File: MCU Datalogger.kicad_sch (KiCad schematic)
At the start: 0 parts

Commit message: Have added required symbols to the schematic sheets
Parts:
- added BT?: Battery, symbol Device:Battery
- added C? (x4): C, symbol Device:C
- added C?: C_Polarized, symbol Device:C_Polarized
- added D? (x2): LED, symbol Device:LED
- added H? (x4): MountingHole, symbol Mechanical:MountingHole
- added R1, R2, R3, R4, R5, R? (x2): R, symbol Device:R
- added U1, U2: 24LC1025, symbol Memory_EEPROM:24LC1025
- added U?: DS1337S+, SOIC127P600X175-8N, symbol DS1337S_:DS1337S+
- added U?: ATMEGA328P-AU, QFP80P900X900X120-32N, symbol ATMEGA328P-AU:ATMEGA328P-AU
- added Y? (x2): Crystal, symbol Device:Crystal
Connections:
- new net: U?.21 (GND), U?.3 (GND), U?.5 (GND)
- new net: U?.4 (VCC), U?.6 (VCC)
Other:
- added sheet Connectors (connectors.kicad_sch)

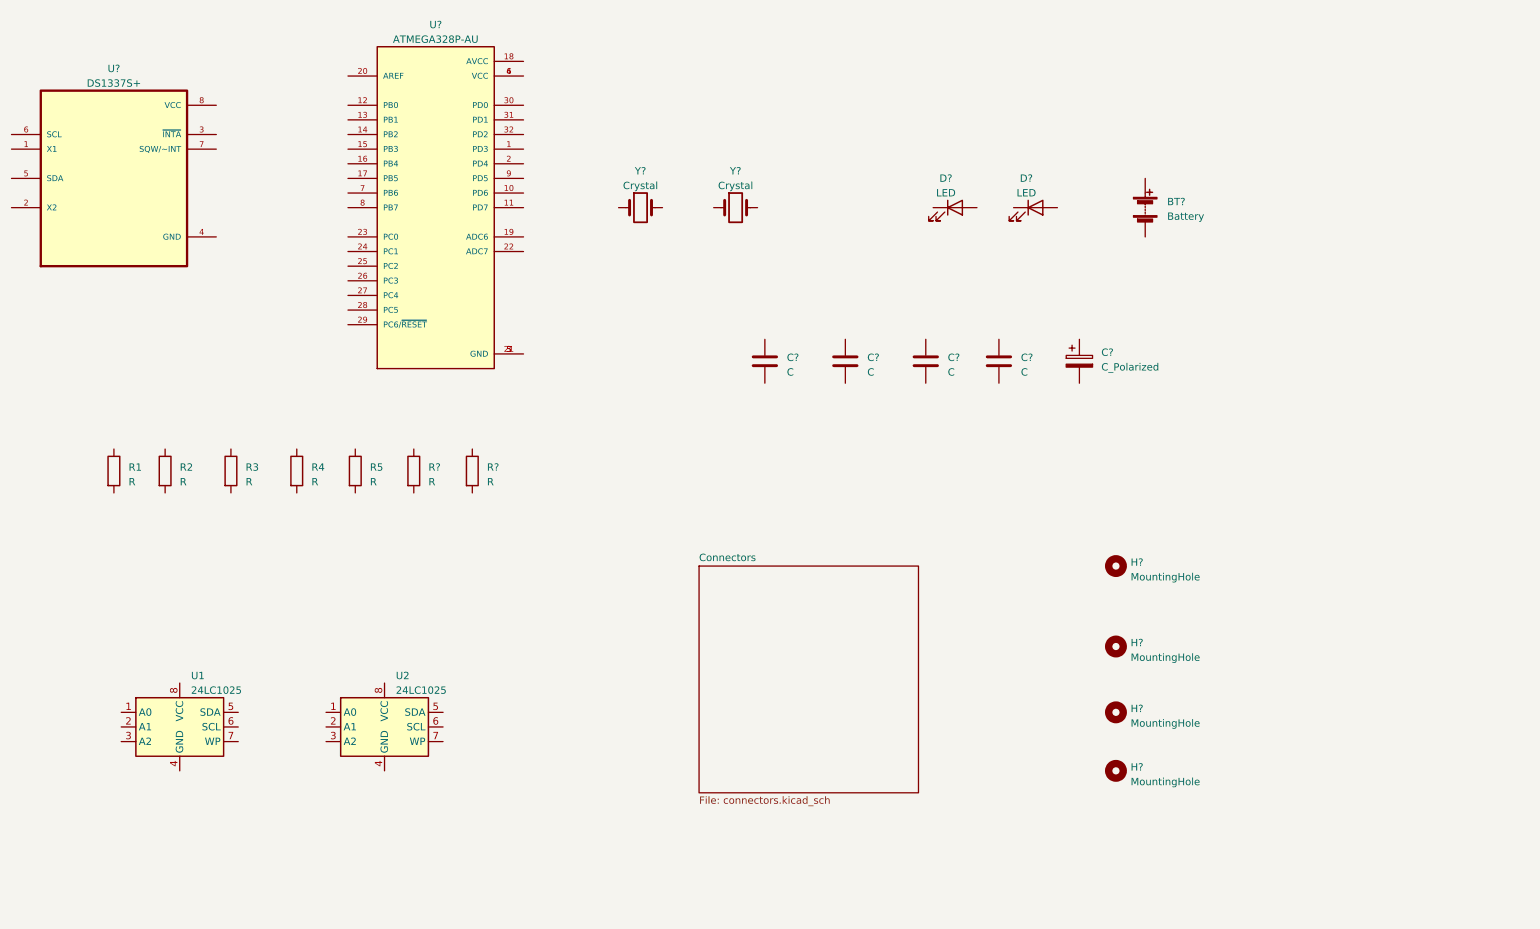
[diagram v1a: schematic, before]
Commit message: Changed locations of symbols (arrange)
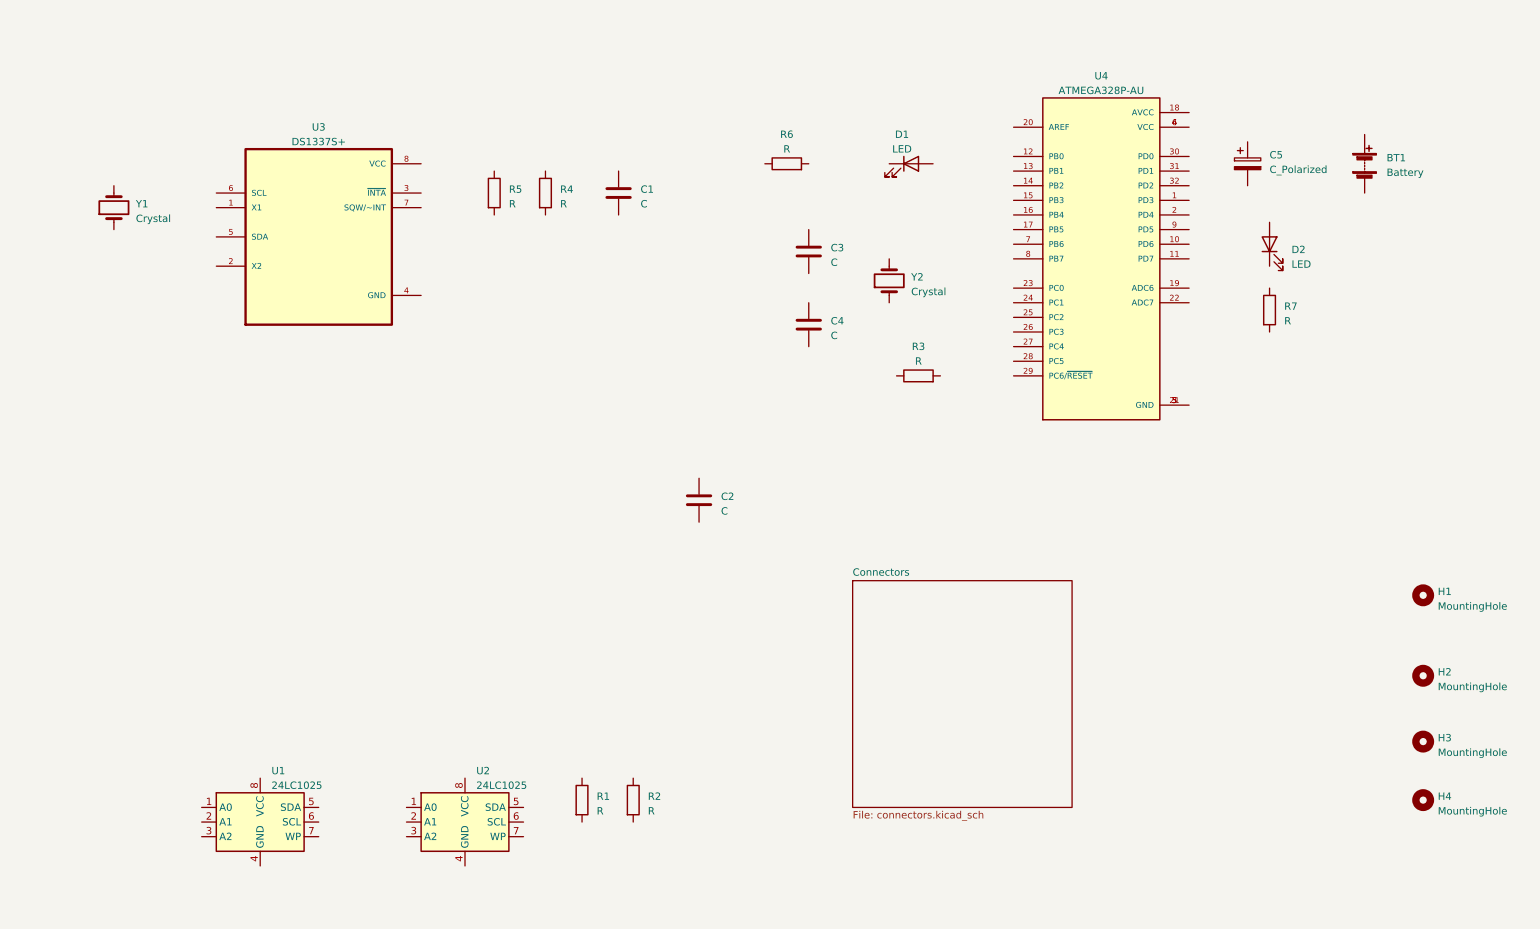
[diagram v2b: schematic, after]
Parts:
- gave numbers to parts that had none: 18
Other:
- moved on the sheet: BT1, C1, C2, C3, C4, C5, D1, D2, H1, H2, H3, H4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

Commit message: Added component values
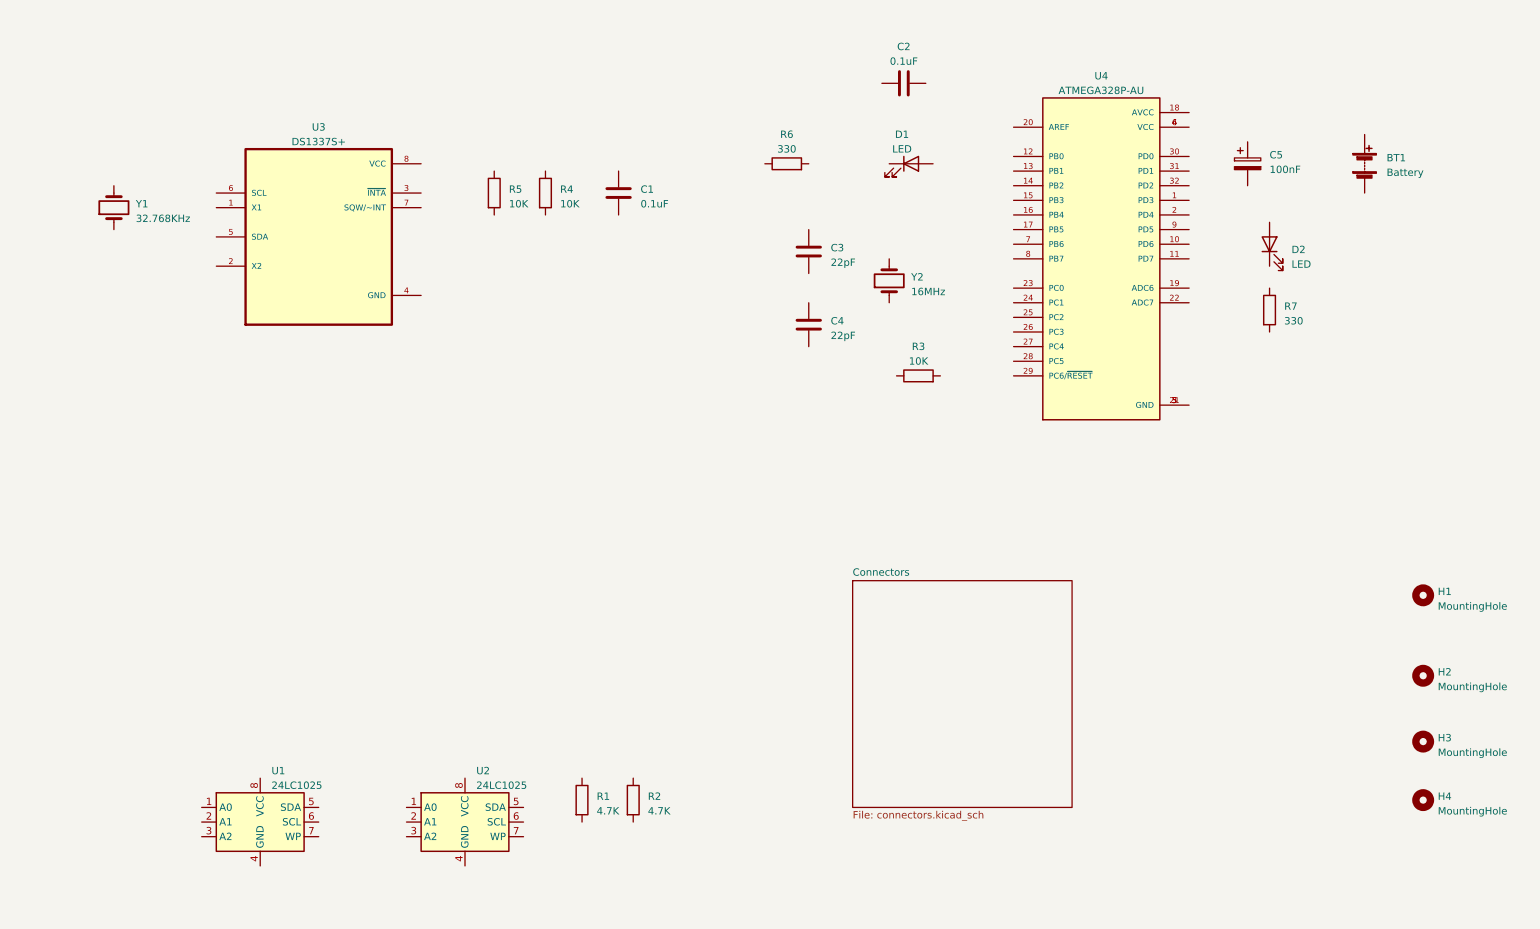
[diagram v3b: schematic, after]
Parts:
- C1, C2: value C -> 0.1uF
- C3, C4: value C -> 22pF
- C5: value C_Polarized -> 100nF
- R1, R2: value R -> 4.7K
- R3, R4, R5: value R -> 10K
- R6, R7: value R -> 330
- Y1: value Crystal -> 32.768KHz
- Y2: value Crystal -> 16MHz
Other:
- moved on the sheet: C2
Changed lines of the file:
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@@
       (effects (font (size 1.27 1.27)) (justify left))
     )
-    (property "Value" "R" (at 104.14 50.165 0)
+    (property "Value" "10K" (at 104.14 50.165 0)
       (effects (font (size 1.27 1.27)) (justify left))
     )
@@
       (effects (font (size 1.27 1.27)) (justify left))
     )
-    (property "Value" "C" (at 160.02 60.325 0)
+    (property "Value" "22pF" (at 160.02 60.325 0)
       (effects (font (size 1.27 1.27)) (justify left))
     )
@@
       (effects (font (size 1.27 1.27)) (justify left))
     )
-    (property "Value" "R" (at 238.76 70.485 0)
+    (property "Value" "330" (at 238.76 70.485 0)
       (effects (font (size 1.27 1.27)) (justify left))
     )
@@
       (effects (font (size 1.27 1.27)) (justify left))
     )
-    (property "Value" "C" (at 127 50.165 0)
+    (property "Value" "0.1uF" (at 127 50.165 0)
       (effects (font (size 1.27 1.27)) (justify left))
     )
@@
       (effects (font (size 1.27 1.27)) (justify left))
     )
-    (property "Value" "R" (at 119.38 155.575 0)
+    (property "Value" "4.7K" (at 119.38 155.575 0)
       (effects (font (size 1.27 1.27)) (justify left))
     )
@@
       (effects (font (size 1.27 1.27)) (justify left))
     )
-    (property "Value" "R" (at 128.27 155.575 0)
+    (property "Value" "4.7K" (at 128.27 155.575 0)
       (effects (font (size 1.27 1.27)) (justify left))
     )
@@
       (effects (font (size 1.27 1.27)) (justify left))
     )
-    (property "Value" "C_Polarized" (at 236.22 44.196 0)
+    (property "Value" "100nF" (at 236.22 44.196 0)
       (effects (font (size 1.27 1.27)) (justify left))
     )
@@
     (property "Datasheet" "~" (at 232.41 43.18 0)
       (effects (font (size 1.27 1.27)) hide)
+    )
+    (property "Purpose" "" (at 232.41 43.18 0)
+      (effects (font (size 1.27 1.27)))
     )
     (pin "1")
@@
       (effects (font (size 1.27 1.27)) (justify right))
     )
-    (property "Value" "Crystal" (at 39.37 52.705 90)
+    (property "Value" "32.768KHz" (at 39.37 52.705 90)
       (effects (font (size 1.27 1.27)) (justify right))
     )
@@
     (property "Datasheet" "~" (at 35.56 50.8 0)
       (effects (font (size 1.27 1.27)) hide)
+    )
+    (property "Purpose" "" (at 35.56 50.8 0)
+      (effects (font (size 1.27 1.27)))
     )
     (pin "1")
@@
       (effects (font (size 1.27 1.27)) (justify left))
     )
-    (property "Value" "R" (at 113.03 50.165 0)
+    (property "Value" "10K" (at 113.03 50.165 0)
       (effects (font (size 1.27 1.27)) (justify left))
     )
@@
       (effects (font (size 1.27 1.27)))
     )
-    (property "Value" "R" (at 175.26 77.47 90)
+    (property "Value" "10K" (at 175.26 77.47 90)
       (effects (font (size 1.27 1.27)))
     )
@@
     )
   )
-  (symbol (lib_id "Device:C") (at 137.16 101.6 0) (unit 1)
-    (in_bom yes) (on_board yes) (dnp no) (fields_autoplaced)
-    (property "Reference" "C2" (at 140.97 100.965 0)
-      (effects (font (size 1.27 1.27)) (justify left))
-    )
-    (property "Value" "C" (at 140.97 103.505 0)
-      (effects (font (size 1.27 1.27)) (justify left))
-    )
-    (property "Footprint" "" (at 138.1252 105.41 0)
-      (effects (font (size 1.27 1.27)) hide)
-    )
-    (property "Datasheet" "~" (at 137.16 101.6 0)
+  (symbol (lib_id "Device:C") (at 172.72 29.21 90) (unit 1)
+    (in_bom yes) (on_board yes) (dnp no) (fields_autoplaced)
+    (property "Reference" "C2" (at 172.72 22.86 90)
+      (effects (font (size 1.27 1.27)))
+    )
+    (property "Value" "0.1uF" (at 172.72 25.4 90)
+      (effects (font (size 1.27 1.27)))
+    )
+    (property "Footprint" "" (at 176.53 28.2448 0)
+      (effects (font (size 1.27 1.27)) hide)
+    )
+    (property "Datasheet" "~" (at 172.72 29.21 0)
       (effects (font (size 1.27 1.27)) hide)
     )
@@
       (effects (font (size 1.27 1.27)) (justify right))
     )
-    (property "Value" "Crystal" (at 173.99 65.405 90)
+    (property "Value" "16MHz" (at 173.99 65.405 90)
       (effects (font (size 1.27 1.27)) (justify right))
     )
@@
       (effects (font (size 1.27 1.27)))
     )
-    (property "Value" "R" (at 152.4 40.64 90)
+    (property "Value" "330" (at 152.4 40.64 90)
       (effects (font (size 1.27 1.27)))
     )
@@
       (effects (font (size 1.27 1.27)) (justify left))
     )
-    (property "Value" "C" (at 160.02 73.025 0)
-      (effects (font (size 1.27 1.27)) (justify left))
-    )
+    (property "Value" "22pF" (at 160.02 73.025 0)
+      (effects (font (size 1.27 1.27)) (justify left))
+    )

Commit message: Completed symbol-footprint associations
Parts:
- BT1: footprint (none) -> Connector_PinHeader_2.54mm:PinHeader_1x02_P2.54mm_Vertical
- C1, C2, C3, C4, C5: footprint (none) -> Capacitor_SMD:C_0805_2012Metric
- D1, D2: footprint (none) -> LED_SMD:LED_0805_2012Metric
- H1, H2, H3, H4: footprint (none) -> MountingHole:MountingHole_2.1mm
- R1, R2, R3, R4, R5, R6, R7: footprint (none) -> Resistor_SMD:R_0805_2012Metric
- U1, U2: footprint (none) -> Package_SO:SOIC-8_5.23x5.23mm_P1.27mm
- U3: footprint SOIC127P600X175-8N -> Footprints:SOIC127P600X175-8N
- U4: footprint QFP80P900X900X120-32N -> Footprints:QFP80P900X900X120-32N
- Y1, Y2: footprint (none) -> Crystal:Crystal_SMD_5032-2Pin_5.0x3.2mm_HandSoldering
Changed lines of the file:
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@@
       (effects (font (size 1.27 1.27)) (justify left))
     )
-    (property "Footprint" "" (at 99.822 48.26 90)
+    (property "Footprint" "Resistor_SMD:R_0805_2012Metric" (at 99.822 48.26 90)
       (effects (font (size 1.27 1.27)) hide)
     )
@@
       (effects (font (size 1.27 1.27)) (justify left))
     )
-    (property "Footprint" "" (at 262.89 118.11 0)
+    (property "Footprint" "MountingHole:MountingHole_2.1mm" (at 262.89 118.11 0)
       (effects (font (size 1.27 1.27)) hide)
     )
@@
       (effects (font (size 1.27 1.27)) (justify left))
     )
-    (property "Footprint" "" (at 157.1752 62.23 0)
+    (property "Footprint" "Capacitor_SMD:C_0805_2012Metric" (at 157.1752 62.23 0)
       (effects (font (size 1.27 1.27)) hide)
     )
@@
       (effects (font (size 1.27 1.27)) (justify left))
     )
-    (property "Footprint" "" (at 234.442 68.58 90)
+    (property "Footprint" "Resistor_SMD:R_0805_2012Metric" (at 234.442 68.58 90)
       (effects (font (size 1.27 1.27)) hide)
     )
@@
       (effects (font (size 1.27 1.27)) (justify right))
     )
-    (property "Footprint" "" (at 236.22 57.15 0)
+    (property "Footprint" "LED_SMD:LED_0805_2012Metric" (at 236.22 57.15 0)
       (effects (font (size 1.27 1.27)) hide)
     )
@@
       (effects (font (size 1.27 1.27)) (justify left))
     )
-    (property "Footprint" "" (at 124.1552 52.07 0)
+    (property "Footprint" "Capacitor_SMD:C_0805_2012Metric" (at 124.1552 52.07 0)
       (effects (font (size 1.27 1.27)) hide)
     )
@@
       (effects (font (size 1.27 1.27)) (justify left))
     )
-    (property "Footprint" "" (at 115.062 153.67 90)
+    (property "Footprint" "Resistor_SMD:R_0805_2012Metric" (at 115.062 153.67 90)
       (effects (font (size 1.27 1.27)) hide)
     )
@@
       (effects (font (size 1.27 1.27)) (justify left))
     )
-    (property "Footprint" "" (at 123.952 153.67 90)
+    (property "Footprint" "Resistor_SMD:R_0805_2012Metric" (at 123.952 153.67 90)
       (effects (font (size 1.27 1.27)) hide)
     )
@@
       (effects (font (size 1.27 1.27)) (justify left))
     )
-    (property "Footprint" "" (at 233.3752 46.99 0)
+    (property "Footprint" "Capacitor_SMD:C_0805_2012Metric" (at 233.3752 46.99 0)
       (effects (font (size 1.27 1.27)) hide)
     )
@@
       (effects (font (size 1.27 1.27)))
     )
-    (property "Footprint" "" (at 173.99 43.18 0)
+    (property "Footprint" "LED_SMD:LED_0805_2012Metric" (at 173.99 43.18 0)
       (effects (font (size 1.27 1.27)) hide)
     )
@@
       (effects (font (size 1.27 1.27)) (justify right))
     )
-    (property "Footprint" "" (at 35.56 50.8 0)
+    (property "Footprint" "Crystal:Crystal_SMD_5032-2Pin_5.0x3.2mm_HandSoldering" (at 35.56 50.8 0)
       (effects (font (size 1.27 1.27)) hide)
     )
@@
       (effects (font (size 1.27 1.27)))
     )
-    (property "Footprint" "SOIC127P600X175-8N" (at 71.12 55.88 0)
+    (property "Footprint" "Footprints:SOIC127P600X175-8N" (at 71.12 55.88 0)
       (effects (font (size 1.27 1.27)) (justify bottom) hide)
     )
@@
       (effects (font (size 1.27 1.27)) (justify left))
     )
-    (property "Footprint" "" (at 108.712 48.26 90)
+    (property "Footprint" "Resistor_SMD:R_0805_2012Metric" (at 108.712 48.26 90)
       (effects (font (size 1.27 1.27)) hide)
     )
@@
       (effects (font (size 1.27 1.27)) (justify left))
     )
-    (property "Footprint" "" (at 252.73 41.656 90)
+    (property "Footprint" "Connector_PinHeader_2.54mm:PinHeader_1x02_P2.54mm_Vertical" (at 252.73 41.656 90)
       (effects (font (size 1.27 1.27)) hide)
     )
@@
       (effects (font (size 1.27 1.27)))
     )
-    (property "Footprint" "" (at 175.26 81.788 90)
+    (property "Footprint" "Resistor_SMD:R_0805_2012Metric" (at 175.26 81.788 90)
       (effects (font (size 1.27 1.27)) hide)
     )
@@
       (effects (font (size 1.27 1.27)))
     )
-    (property "Footprint" "QFP80P900X900X120-32N" (at 207.01 59.69 0)
+    (property "Footprint" "Footprints:QFP80P900X900X120-32N" (at 207.01 59.69 0)
       (effects (font (size 1.27 1.27)) (justify bottom) hide)
     )
@@
       (effects (font (size 1.27 1.27)) (justify left))
     )
-    (property "Footprint" "" (at 262.89 143.51 0)
+    (property "Footprint" "MountingHole:MountingHole_2.1mm" (at 262.89 143.51 0)
       (effects (font (size 1.27 1.27)) hide)
     )
@@
       (effects (font (size 1.27 1.27)) (justify left))
     )
-    (property "Footprint" "" (at 60.96 157.48 0)
+    (property "Footprint" "Package_SO:SOIC-8_5.23x5.23mm_P1.27mm" (at 60.96 157.48 0)
       (effects (font (size 1.27 1.27)) hide)
     )
@@
       (effects (font (size 1.27 1.27)) (justify left))
     )
-    (property "Footprint" "" (at 262.89 153.67 0)
+    (property "Footprint" "MountingHole:MountingHole_2.1mm" (at 262.89 153.67 0)
       (effects (font (size 1.27 1.27)) hide)
     )
@@
       (effects (font (size 1.27 1.27)))
     )
-    (property "Footprint" "" (at 176.53 28.2448 0)
+    (property "Footprint" "Capacitor_SMD:C_0805_2012Metric" (at 176.53 28.2448 0)
       (effects (font (size 1.27 1.27)) hide)
     )
@@
       (effects (font (size 1.27 1.27)) (justify right))
     )
-    (property "Footprint" "" (at 170.18 63.5 0)
+    (property "Footprint" "Crystal:Crystal_SMD_5032-2Pin_5.0x3.2mm_HandSoldering" (at 170.18 63.5 0)
       (effects (font (size 1.27 1.27)) hide)
     )
@@
       (effects (font (size 1.27 1.27)))
     )
-    (property "Footprint" "" (at 152.4 44.958 90)
+    (property "Footprint" "Resistor_SMD:R_0805_2012Metric" (at 152.4 44.958 90)
       (effects (font (size 1.27 1.27)) hide)
     )
@@
       (effects (font (size 1.27 1.27)) (justify left))
     )
-    (property "Footprint" "" (at 157.1752 74.93 0)
+    (property "Footprint" "Capacitor_SMD:C_0805_2012Metric" (at 157.1752 74.93 0)
       (effects (font (size 1.27 1.27)) hide)
     )
@@
       (effects (font (size 1.27 1.27)) (justify left))
     )
-    (property "Footprint" "" (at 96.52 157.48 0)
+    (property "Footprint" "Package_SO:SOIC-8_5.23x5.23mm_P1.27mm" (at 96.52 157.48 0)
       (effects (font (size 1.27 1.27)) hide)
     )
@@
       (effects (font (size 1.27 1.27)) (justify left))
     )
-    (property "Footprint" "" (at 262.89 132.08 0)
-      (effects (font (size 1.27 1.27)) hide)
-    )
+    (property "Footprint" "MountingHole:MountingHole_2.1mm" (at 262.89 132.08 0)
+      (effects (font (size 1.27 1.27)) hide)
+    )
